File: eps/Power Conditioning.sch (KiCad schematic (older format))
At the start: 16 parts, among them U1 ADP2303ARDZ-3.3, U2 ADP2303ARDZ-5.0, U3 CS5172EDR8G

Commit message: implement uvp/ovp
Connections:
- net labels added: PCM_IN_FILT
- net labels removed: PCM_IN
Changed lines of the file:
@@
 	5300 2550 5200 2550
 Connection ~ 6250 2350
-Text Label 3700 3350 2    50   ~ 0
-PCM_IN
-Text Label 3700 2150 2    50   ~ 0
-PCM_IN
 $Comp
 L power:+3.3V #PWR?
@@
 	1    0    0    -1
 $EndComp
+Text GLabel 3700 2150 0    50   Input ~ 0
+PCM_IN_FILT
+Text GLabel 3700 3350 0    50   Input ~ 0
+PCM_IN_FILT
 $EndSCHEMATC

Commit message: current limiters
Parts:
- added C10, C9: 10uF, symbol Device:CP
- added C11, C14, C15: 1uF, symbol Device:C
- added C12, C13, C16: 0.1uF, symbol Device:C
- added C8: 100uF, symbol Device:CP
- added Q18: IRLZ44N, Package_TO_SOT_THT:TO-220-3_Vertical, symbol Transistor_FET:IRLZ44N
- added Q19, Q20, Q21: IRF4905, Package_TO_SOT_THT:TO-220-3_Vertical, symbol Transistor_FET:IRF4905
- added Q22, Q23, Q24: 2N7002, Package_TO_SOT_SMD:SOT-23, symbol Transistor_FET:2N7002
- added R28: 322K, symbol Device:R
- added R29: 678K, symbol Device:R
- added R30: 11.2M, symbol Device:R
- added R31: 100K, symbol Device:R_Small
- added R32, R33, R36, R37, R38, R41, R42, R46, R48, R49, R50, R51: 10K, symbol Device:R
- added R34, R43, R44: 15m, symbol Device:R
- added R35: 65K, symbol Device:R
- added R45, R47: 27K, symbol Device:R
- added U5: LTC4365TS8, symbol Power_Management:LTC4365TS8
- added U6: LM1117-5.0, symbol Regulator_Linear:LM1117-5.0
- added U7, U8, U9: MAX4373F, symbol epslib:MAX4373
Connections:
- net labels added: +BATT, 3V3GATE, 3V3RAW, 5VGATE, BATGATE, FAULT, FIX_5V, GND, I3V3, I5V, IBATV, PCM_IN, RST3V3, RST5V, RSTBATT, VCC
- wire segments 39 -> 114
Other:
- note added: "3A CURRENT LIMIT (LATCHING W/ RESET PIN)"
- note added: "3v3 BUCK"
- note added: "5v BUCK"
- note added: "6A CURRENT LIMIT (LATCHING W/ RESET PIN)"
- note added: "Low current constant-on 5V line for constant VCC"
- note added: "UVP/OVP set to 6.2V and 9V respectively"
- note added: "uC and i2c node powered from 3v3raw to be able to reset ocp"
- moved on the sheet: C1, C2, C3, C4, C5, C6, C7, D1, D2, L1, L2, R39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

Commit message: add pcm resets
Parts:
- removed U3: CS5172EDR8G, symbol epslib:CS5172EDR8G
- added Q25, Q26: 2N7002, Package_TO_SOT_SMD:SOT-23, symbol Transistor_FET:2N7002
- added R52, R53: 10K, symbol Device:R_Small
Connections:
- net labels added: 3V3RESETPLS, 3v3gate, 5VRESETPLS
- net labels removed: 3V3GATE, BATGATE
- wire segments 114 -> 128
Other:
- moved on the sheet: C1, C11, C16, C2, Q22, R32, R33, R34, R35, R36, R38, U7

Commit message: switch vcc to 3.3v, add battery switching mosfet
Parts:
- removed U6: LM1117-5.0, symbol Regulator_Linear:LM1117-5.0
- added Q27: 2N7002, Package_TO_SOT_SMD:SOT-23, symbol Transistor_FET:2N7002
- added R60: 10K, symbol Device:R_Small
- added U6: LM1117-3.3, symbol Regulator_Linear:LM1117-3.3
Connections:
- net labels added: BATGATE, BATRESETPLS, FIX_3V3
- net labels removed: FIX_5V
- wire segments 128 -> 135
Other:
- note added: "Low current constant-on 3V3 line for constant VCC"
- note removed: "Low current constant-on 5V line for constant VCC"
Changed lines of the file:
@@
 $EndComp
 Text Label 2450 3150 0    50   ~ 0
-FIX_5V
+FIX_3V3
 Wire Wire Line
 	2250 3150 2450 3150
@@
 $EndComp
 Text Notes 850  2850 0    50   ~ 0
-Low current constant-on 5V line for constant VCC
-$Comp
-L Regulator_Linear:LM1117-5.0 U6
-U 1 1 6183C32C
-P 1950 3150
-F 0 "U6" H 1950 3392 50  0000 C CNN
-F 1 "LM1117-5.0" H 1950 3301 50  0000 C CNN
-F 2 "" H 1950 3150 50  0001 C CNN
-F 3 "http://www.ti.com/lit/ds/symlink/lm1117.pdf" H 1950 3150 50  0001 C CNN
-	1    1950 3150
-	1    0    0    -1
-$EndComp
+Low current constant-on 3V3 line for constant VCC
 $Comp
 L Transistor_FET:IRF4905 Q21
@@
 Text Notes 6600 4350 0    50   ~ 0
 3A CURRENT LIMIT (LATCHING W/ RESET PIN)
-Text Notes 3800 6050 0    50   ~ 0
+Text Notes 4750 6400 0    50   ~ 0
 6A CURRENT LIMIT (LATCHING W/ RESET PIN)
 Text Notes 5850 650  0    50   ~ 0
@@
 $EndSheet
 $Sheet
-S 3950 6350 650  300
+S 4300 6600 650  300
 U 619D4C5F
 F0 "BAT RESET" 50
 F1 "Pulse500ms.sch" 50
-F2 "pulse" I L 3950 6500 50
-F3 "gate" I L 3950 6400 50
+F2 "pulse" I L 4300 6750 50
+F3 "gate" I L 4300 6650 50
 $EndSheet
 Text Label 4300 2000 2    50   ~ 0
@@
 Text GLabel 4400 4150 0    50   Input ~ 0
 5VRESETPLS
+$Comp
+L Regulator_Linear:LM1117-3.3 U6
+U 1 1 61827DCE
+P 1950 3150
+F 0 "U6" H 1950 3392 50  0000 C CNN
+F 1 "LM1117-3.3" H 1950 3301 50  0000 C CNN
+F 2 "" H 1950 3150 50  0001 C CNN
+F 3 "http://www.ti.com/lit/ds/symlink/lm1117.pdf" H 1950 3150 50  0001 C CNN
+	1    1950 3150
+	1    0    0    -1
+$EndComp
+Text GLabel 4300 6750 0    50   Input ~ 0
+BATRESETPLS
+$Comp
+L Transistor_FET:2N7002 Q27
+U 1 1 618500FB
+P 4200 5950
+F 0 "Q27" H 4405 5996 50  0000 L CNN
+F 1 "2N7002" H 4405 5905 50  0000 L CNN
+F 2 "Package_TO_SOT_SMD:SOT-23" H 4400 5875 50  0001 L CIN
+F 3 "https://www.onsemi.com/pub/Collateral/NDS7002A-D.PDF" H 4200 5950 50  0001 L CNN
+	1    4200 5950
+	1    0    0    -1
+$EndComp
+Wire Wire Line
+	4500 5350 4500 5500
+Wire Wire Line
+	4500 5500 4300 5500
+Wire Wire Line
+	4300 5500 4300 5750
+$Comp
+L power:GND #PWR051
+U 1 1 6186D3AF
+P 4300 6150
+F 0 "#PWR051" H 4300 5900 50  0001 C CNN
+F 1 "GND" H 4305 5977 50  0000 C CNN
+F 2 "" H 4300 6150 50  0001 C CNN
+F 3 "" H 4300 6150 50  0001 C CNN
+	1    4300 6150
+	1    0    0    -1
+$EndComp
+Wire Wire Line
+	4300 6650 3900 6650
+Wire Wire Line
+	3900 6650 3900 5950
+Wire Wire Line
+	3900 5950 4000 5950
+Text Label 3900 6650 2    50   ~ 0
+BATGATE
+$Comp
+L Device:R_Small R60
+U 1 1 618945E2
+P 4000 6050
+F 0 "R60" H 4059 6096 50  0000 L CNN
+F 1 "10K" H 4059 6005 50  0000 L CNN
+F 2 "" H 4000 6050 50  0001 C CNN
+F 3 "~" H 4000 6050 50  0001 C CNN
+	1    4000 6050
+	1    0    0    -1
+$EndComp
+Connection ~ 4000 5950
+Wire Wire Line
+	4000 6150 4300 6150
+Connection ~ 4300 6150
 $EndSCHEMATC

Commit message: modify mux, implement hw watchdog, standardize p channel mosfets to irf7425
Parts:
- removed Q19, Q20, Q21: IRF4905, Package_TO_SOT_THT:TO-220-3_Vertical, symbol Transistor_FET:IRF4905
- added Q10, Q7, Q8: IRF7425, Package_SO:SOIC-8_3.9x4.9mm_P1.27mm, symbol Transistor_FET:IRF7404
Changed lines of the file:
@@
 Low current constant-on 3V3 line for constant VCC
-$Comp
-L Transistor_FET:IRF4905 Q21
-U 1 1 6184BF9C
-P 7400 1150
-F 0 "Q21" V 7742 1150 50  0000 C CNN
-F 1 "IRF4905" V 7651 1150 50  0000 C CNN
-F 2 "Package_TO_SOT_THT:TO-220-3_Vertical" H 7600 1075 50  0001 L CIN
-F 3 "http://www.infineon.com/dgdl/irf4905.pdf?fileId=5546d462533600a4015355e32165197c" H 7400 1150 50  0001 L CNN
-	1    7400 1150
-	0    1    -1   0
-$EndComp
 $Comp
 L Device:R R42
@@
 Wire Wire Line
 	8300 1800 8000 1800
-$Comp
-L Transistor_FET:IRF4905 Q20
-U 1 1 618793BE
-P 7000 3200
-F 0 "Q20" V 7342 3200 50  0000 C CNN
-F 1 "IRF4905" V 7251 3200 50  0000 C CNN
-F 2 "Package_TO_SOT_THT:TO-220-3_Vertical" H 7200 3125 50  0001 L CIN
-F 3 "http://www.infineon.com/dgdl/irf4905.pdf?fileId=5546d462533600a4015355e32165197c" H 7000 3200 50  0001 L CNN
-	1    7000 3200
-	0    1    -1   0
-$EndComp
 $Comp
 L Device:R R37
@@
 Wire Wire Line
 	7400 1350 7400 1400
-Connection ~ 7400 1350
 Connection ~ 8750 1050
 Connection ~ 9050 1050
@@
 Wire Wire Line
 	7000 3450 7000 3400
-Connection ~ 7000 3400
 Wire Wire Line
 	7200 3100 8350 3100
-$Comp
-L Transistor_FET:IRF4905 Q19
-U 1 1 61B04E59
-P 4200 4900
-F 0 "Q19" V 4542 4900 50  0000 C CNN
-F 1 "IRF4905" V 4451 4900 50  0000 C CNN
-F 2 "Package_TO_SOT_THT:TO-220-3_Vertical" H 4400 4825 50  0001 L CIN
-F 3 "http://www.infineon.com/dgdl/irf4905.pdf?fileId=5546d462533600a4015355e32165197c" H 4200 4900 50  0001 L CNN
-	1    4200 4900
-	0    1    -1   0
-$EndComp
 $Comp
 L Device:R R32
@@
 Wire Wire Line
 	4200 5150 4200 5100
-Connection ~ 4200 5100
 Wire Wire Line
 	4400 4800 5550 4800
@@
 	4000 6150 4300 6150
 Connection ~ 4300 6150
+$Comp
+L Transistor_FET:IRF7404 Q10
+U 1 1 6185D3C6
+P 7400 1150
+F 0 "Q10" V 7742 1150 50  0000 C CNN
+F 1 "IRF7425" V 7651 1150 50  0000 C CNN
+F 2 "Package_SO:SOIC-8_3.9x4.9mm_P1.27mm" H 7600 1075 50  0001 L CIN
+F 3 "https://www.infineon.com/dgdl/Infineon-IRF7425-DataSheet-v01_01-EN.pdf?fileId=5546d462533600a4015355fb1c361bdc" V 7400 1150 50  0001 L CNN
+	1    7400 1150
+	0    1    -1   0
+$EndComp
+Connection ~ 7400 1350
+$Comp
+L Transistor_FET:IRF7404 Q8
+U 1 1 6187CD62
+P 7000 3200
+F 0 "Q8" V 7342 3200 50  0000 C CNN
+F 1 "IRF7425" V 7251 3200 50  0000 C CNN
+F 2 "Package_SO:SOIC-8_3.9x4.9mm_P1.27mm" H 7200 3125 50  0001 L CIN
+F 3 "https://www.infineon.com/dgdl/Infineon-IRF7425-DataSheet-v01_01-EN.pdf?fileId=5546d462533600a4015355fb1c361bdc" V 7000 3200 50  0001 L CNN
+	1    7000 3200
+	0    1    -1   0
+$EndComp
+$Comp
+L Transistor_FET:IRF7404 Q7
+U 1 1 6188B152
+P 4200 4900
+F 0 "Q7" V 4542 4900 50  0000 C CNN
+F 1 "IRF7425" V 4451 4900 50  0000 C CNN
+F 2 "Package_SO:SOIC-8_3.9x4.9mm_P1.27mm" H 4400 4825 50  0001 L CIN
+F 3 "https://www.infineon.com/dgdl/Infineon-IRF7425-DataSheet-v01_01-EN.pdf?fileId=5546d462533600a4015355fb1c361bdc" V 4200 4900 50  0001 L CNN
+	1    4200 4900
+	0    1    -1   0
+$EndComp
 $EndSCHEMATC

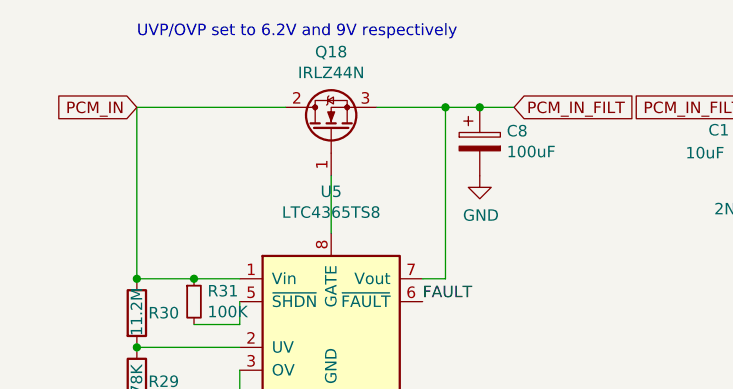
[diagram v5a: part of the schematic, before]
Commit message: replace irlz44n with irf8302
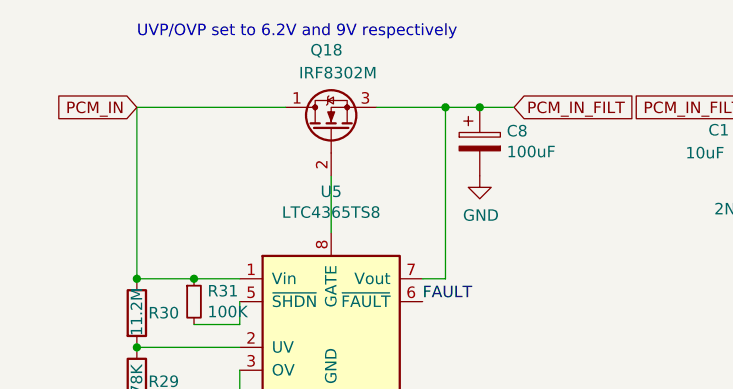
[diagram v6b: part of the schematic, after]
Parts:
- removed Q18: IRLZ44N, Package_TO_SOT_THT:TO-220-3_Vertical, symbol Transistor_FET:IRLZ44N
- added Q18: IRF8302M, Package_DirectFET:DirectFET_MX, symbol Transistor_FET:IRF8302M
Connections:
- net PCM_IN: now also Q18.1 (D)
- net PCM_IN_FILT: now also Q18.3 (S)
- net at U5.8 (GATE): now also Q18.2 (G)
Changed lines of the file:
@@
 	1    0    0    -1
-$EndComp
-$Comp
-L Transistor_FET:IRLZ44N Q18
-U 1 1 6181C665
-P 1950 950
-F 0 "Q18" V 2292 950 50  0000 C CNN
-F 1 "IRLZ44N" V 2201 950 50  0000 C CNN
-F 2 "Package_TO_SOT_THT:TO-220-3_Vertical" H 2200 875 50  0001 L CIN
-F 3 "http://www.irf.com/product-info/datasheets/data/irlz44n.pdf" H 1950 950 50  0001 L CNN
-	1    1950 950
-	0    -1   -1   0
 $EndComp
 Wire Wire Line
@@
 	0    1    -1   0
 $EndComp
+$Comp
+L Transistor_FET:IRF8302M Q18
+U 1 1 6193A157
+P 1950 950
+F 0 "Q18" V 2300 900 50  0000 L CNN
+F 1 "IRF8302M" V 2200 750 50  0000 L CNN
+F 2 "Package_DirectFET:DirectFET_MX" H 1950 950 50  0001 C CIN
+F 3 "https://www.infineon.com/dgdl/irf8302mpbf.pdf?fileId=5546d462533600a40153560d16e41d5b" H 1950 950 50  0001 L CNN
+	1    1950 950
+	0    -1   -1   0
+$EndComp
 $EndSCHEMATC
